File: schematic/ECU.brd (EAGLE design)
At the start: 25 x 79 mm, 21 parts, among them J1 Break, J2 COMM, J3 PWS, J4 DISPLAY, J5 THROTTLE, J6 LED, J7 SPEED, Q1 NMOSFETSOT23, Q5 NMOSFETSOT23

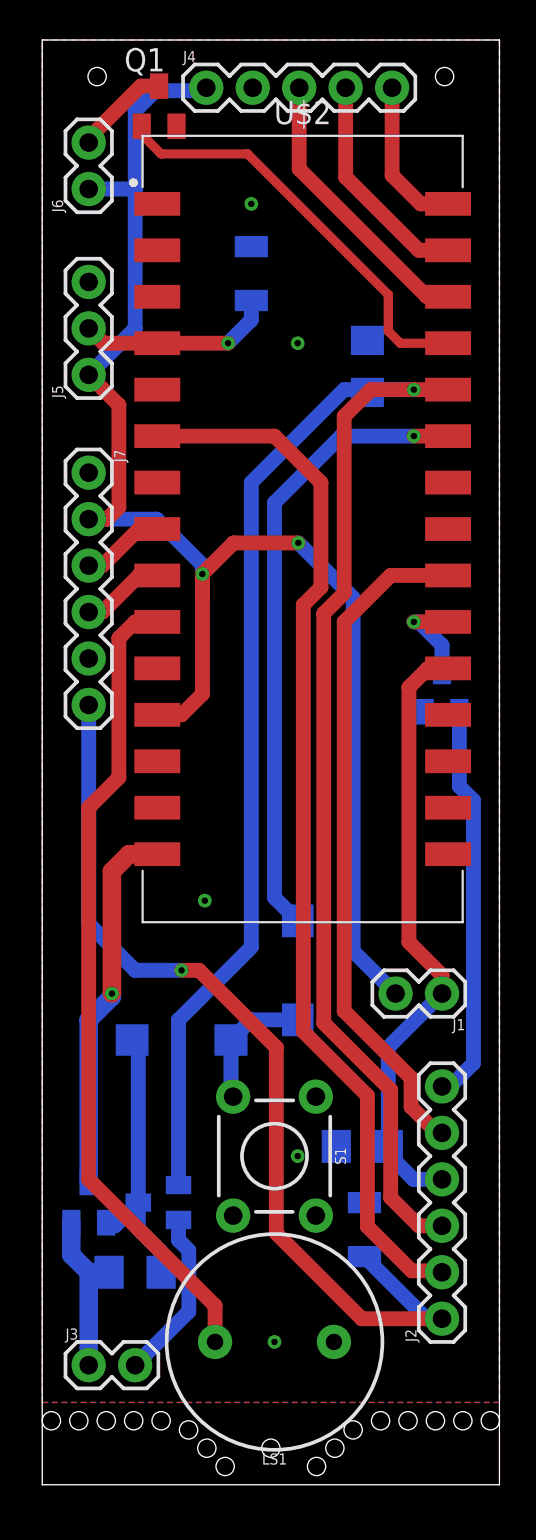
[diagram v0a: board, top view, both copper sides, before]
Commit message: Update schematics
- Add TVS diodes for ESD protection
- Add resistors on MOSFET gates
- Make voltage divider on 2 resistors(4 previously)
- Align signal names on regulator and ECU schematics
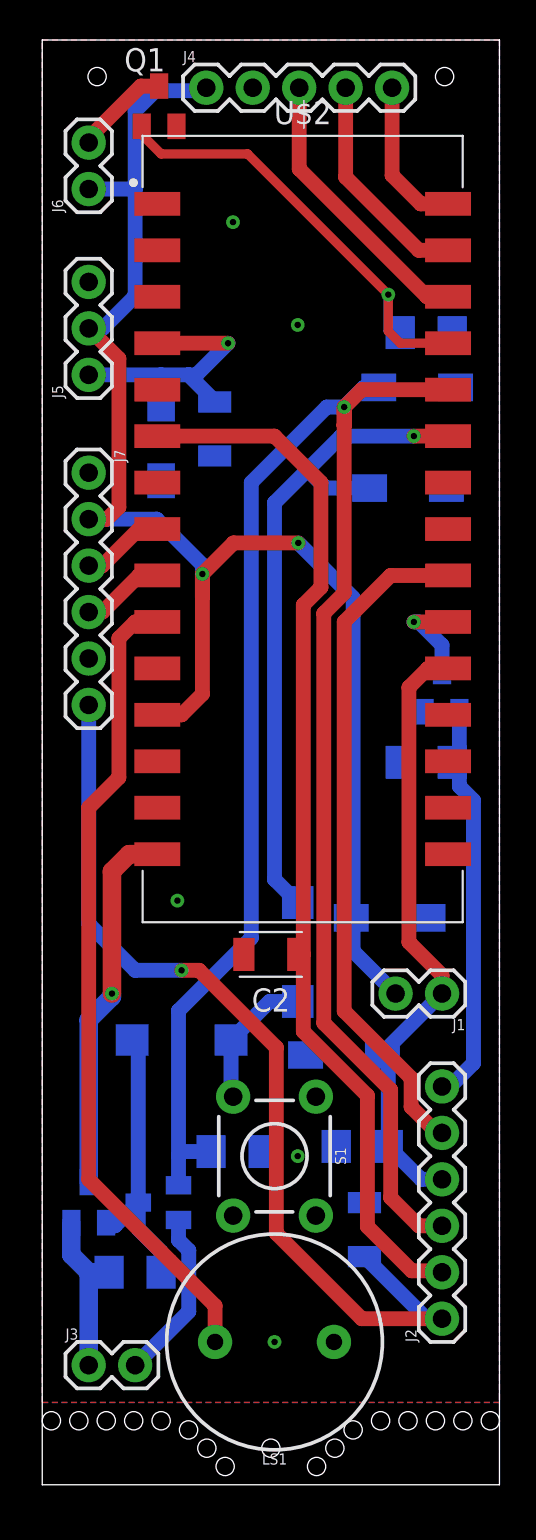
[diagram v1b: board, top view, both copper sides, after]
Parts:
- added C2: (no value), Capacitor:CAPC3216X135
- added D4, D5, D6, D7, U$1: TVS_DIODESMA, eScooter:DIOM5027X220N
- added R4, R5: 10K, eagle-ltspice:R1206
- moved R1 43.5 mm to (10.7, 18.2), turned to 0 degrees
- moved C1 8.73 mm to (9.43, 57.7), turned to 90 degrees
- moved D3 1.00 mm to (14.0, 29.1)
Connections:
- removed net PWR: J2.3, Q2.1, R1.2, U$2.26
- new net PWM: D7.1, J2.3, Q2.1, R1.2, U$2.26
- net 5V: now also D6.1, J5.2; no longer J5.1
- net BAT: now also C2.1
- net BTN: now also U$1.2
- net GND: now also C2.2, D4.1, D5.1, D6.2, D7.2, R4.1, R5.1, U$1.1
- net LEDCTL: now also R5.2
- net SPIN: now also R4.2
- net ST: now also D5.2
- net THIN: now also D4.2, J5.1; no longer J5.2
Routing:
- net PWM: track 0.00 -> 106.8 mm, vias 0 -> 1
- net PWR: track 105.6 -> 0.00 mm, vias 1 -> 0
- net THIN: track 10.8 -> 15.9 mm
- net BTN: track 34.4 -> 37.2 mm
- net LEDCTL: track 23.1 -> 25.8 mm, vias 0 -> 1
- net 5V: track 83.6 -> 84.1 mm

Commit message: Update schematics for regulator
- Add elements nominals and correct values
- Fix library inconsistence
- Few cosmetical changes in schematics
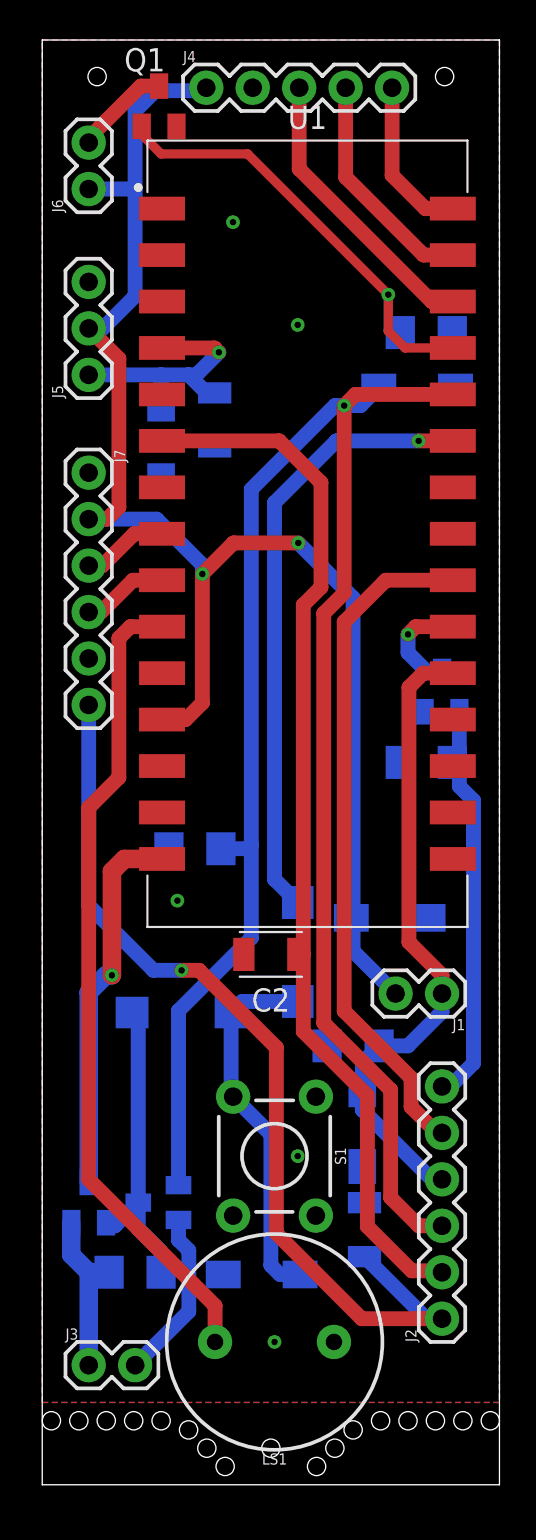
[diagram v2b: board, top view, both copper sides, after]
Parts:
- removed U$1: TVS_DIODESMA, eScooter:DIOM5027X220N
- removed U$2: ARDUINOARDUINO_NANO, regulator:SON254P1750X4300X120-30M
- added D8: TVS_DIODESMA, eScooter:DIOM5027X220N
- added U1: Arduino Nano Every, eScooter:SON254P1750X4300X120-30M
- C1, C2, C3: value (none) -> 0.1uF
- J3: value PWS -> PWR
- R3: value 1M -> 10K
- moved R1 16.7 mm to (8.35, 34.8), turned to 180 degrees
- moved R3 5.52 mm to (17.0, 24.0)
- moved D5 4.12 mm to (17.5, 19.5), turned to 90 degrees
- moved D2 1.50 mm to (7.62, 25.8)
- moved C1 0.50 mm to (9.43, 58.2)
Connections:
- net 3V3: now also U1.2; no longer U$2.2
- net 5V: now also U1.12; no longer U$2.12
- net BAT: now also U1.6; no longer U$2.6
- net BTN: now also U1.25; no longer U$1.2, U$2.25
- net CLK: now also U1.30; no longer U$2.30
- net CS: now also U1.29; no longer U$2.29
- net DIN: now also U1.28; no longer U$2.28
- net GND: now also D8.1, U1.14; no longer U$1.1, U$2.14
- net GND2: now also U1.19; no longer U$2.19
- net LEDCTL: now also U1.27; no longer U$2.27
- net N$5: now also D8.2
- net PWM: now also U1.26; no longer U$2.26
- net SCL: now also U1.9; no longer U$2.9
- net SDA: now also U1.8; no longer U$2.8
- net SP: now also U1.21; no longer U$2.21
- net SPK: now also U1.10; no longer U$2.10
- net ST: now also U1.20; no longer U$2.20
- net STLEDCTL: now also U1.22; no longer U$2.22
- net THIN: now also U1.4; no longer U$2.4
- net VIN: now also U1.15; no longer U$2.15
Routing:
- net N$5: track 7.66 -> 20.4 mm
- net BTN: track 37.2 -> 33.5 mm
- net THIN: track 15.9 -> 14.3 mm
- net N$2: track 15.7 -> 17.2 mm
- net ST: track 33.8 -> 35.2 mm
- net 5V: track 84.1 -> 83.0 mm
- net PWM: track 106.8 -> 105.7 mm
- net SPOUT: track 51.8 -> 51.2 mm

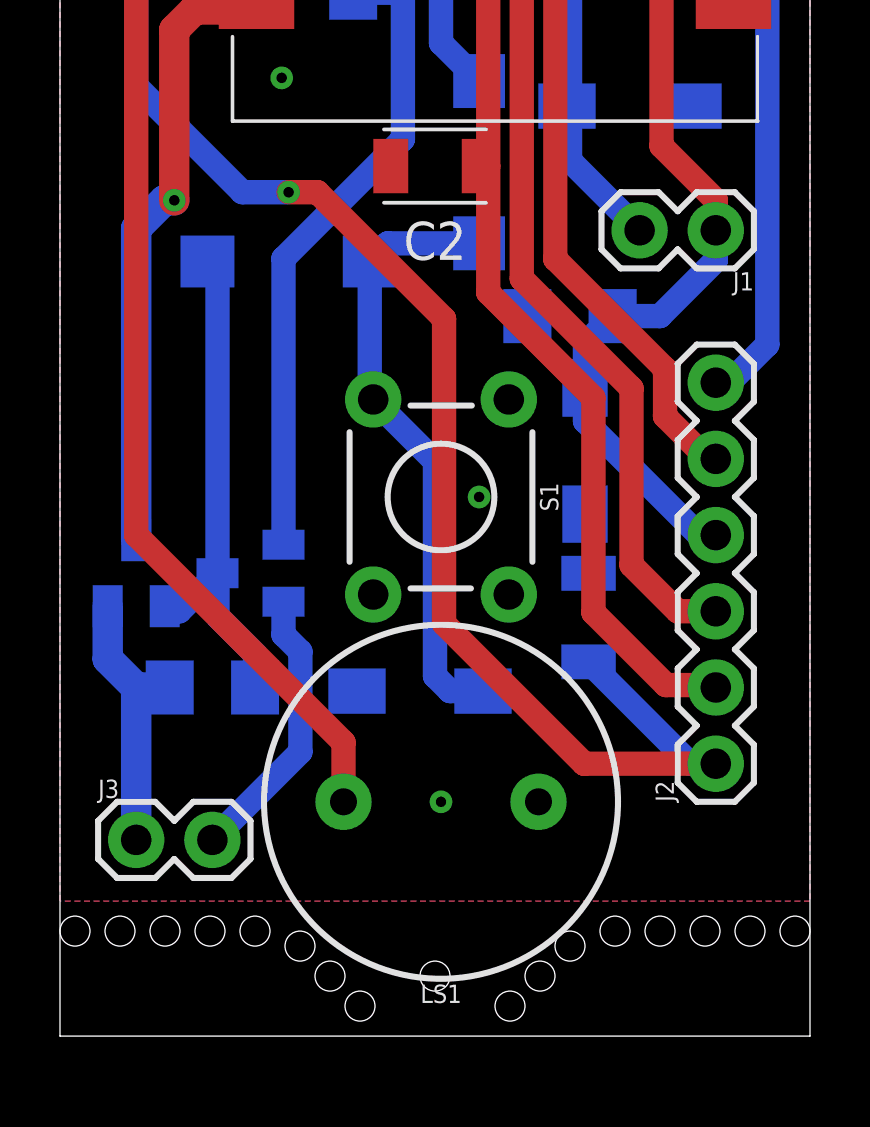
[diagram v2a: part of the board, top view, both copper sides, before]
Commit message: Replace buzzer with 7.6mm contacts spacing
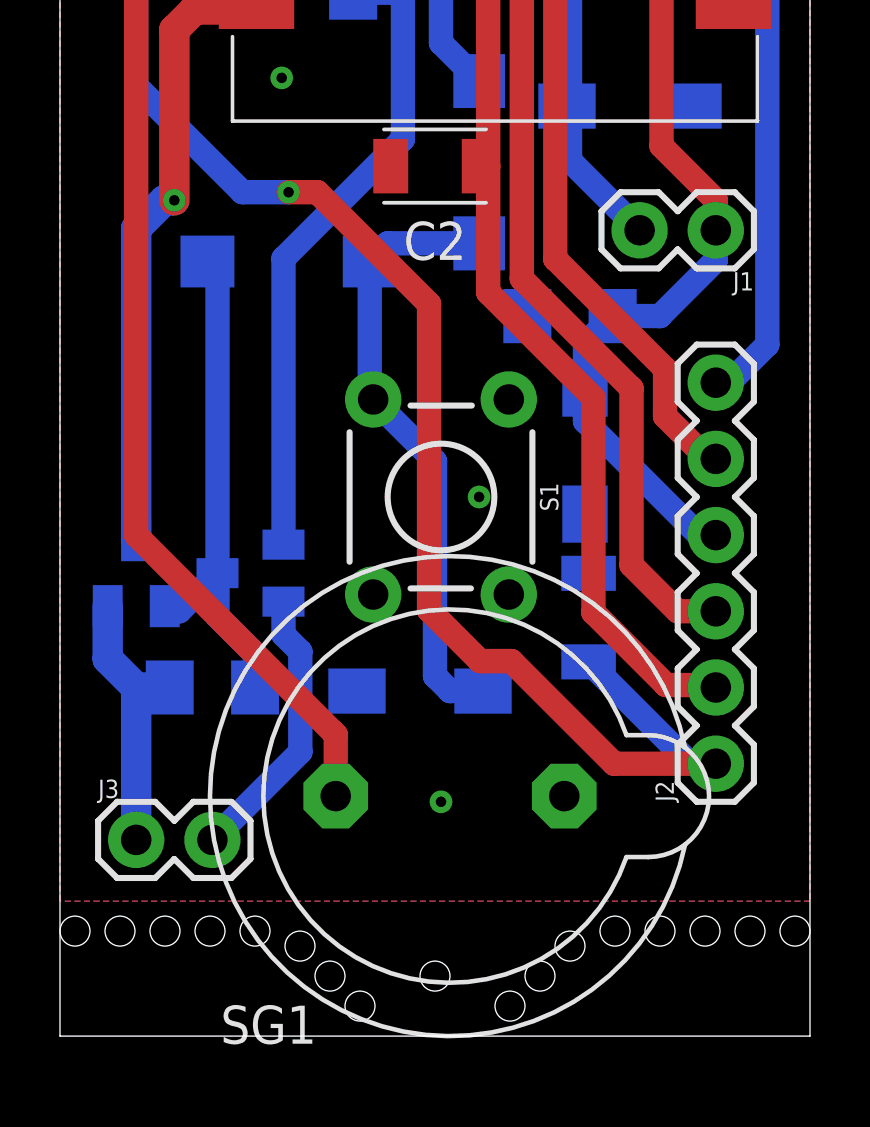
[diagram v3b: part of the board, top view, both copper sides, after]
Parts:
- removed LS1: BUZZER-PTH_KIT, SparkFun-Electromechanical:BUZZER-12MM-KIT
- added SG1: F/HGP, buzzer:F/HGP
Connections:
- net GND: now also SG1.1; no longer LS1.-
- net SPK: now also SG1.2; no longer LS1.+
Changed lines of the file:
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@@
 <attribute name="VALUE" x="9.525" y="17.97" size="0.6096" layer="27" font="vector" ratio="20" rot="R270" align="top-center"/>
-</element>
-<element name="LS1" library="SparkFun-Electromechanical" library_urn="urn:adsk.eagle:library:516" package="BUZZER-12MM-KIT" package3d_urn="urn:adsk.eagle:package:38556/1" value="BUZZER-PTH_KIT" x="12.7" y="7.81" smashed="yes" rot="R180">
-<attribute name="NAME" x="12.7" y="1.714" size="0.6096" layer="25" font="vector" ratio="20" rot="R180" align="bottom-center"/>
-<attribute name="PROD_ID" value="COMP-08253" x="12.7" y="7.81" size="1.778" layer="27" rot="R180" display="off"/>
-<attribute name="SF_SKU" value="COM-07950" x="12.7" y="7.81" size="1.778" layer="27" rot="R180" display="off"/>
-<attribute name="VALUE" x="12.7" y="2.222" size="0.6096" layer="27" font="vector" ratio="20" rot="R180" align="top-center"/>
 </element>
 <element name="R3" library="eagle-ltspice" library_urn="urn:adsk.eagle:library:217" package="R1206" package3d_urn="urn:adsk.eagle:package:13301/1" value="10K" x="17" y="24" smashed="yes" rot="MR0">
@@
 <attribute name="NAME" x="14.5" y="74.135" size="1.27" layer="25" align="bottom-center"/>
 <attribute name="VALUE" x="14.5" y="29.865" size="1.27" layer="27" align="top-center"/>
+</element>
+<element name="SG1" library="buzzer" library_urn="urn:adsk.eagle:library:113" package="F/HGP" package3d_urn="urn:adsk.eagle:package:5287/1" value="F/HGP" x="13" y="8" smashed="yes" rot="R180">
+<attribute name="MF" value="" x="13" y="8" size="1.778" layer="27" rot="R180" display="off"/>
+<attribute name="MPN" value="" x="13" y="8" size="1.778" layer="27" rot="R180" display="off"/>
+<attribute name="NAME" x="8.555" y="1.015" size="1.27" layer="25" ratio="10" rot="R180"/>
+<attribute name="OC_FARNELL" value="unknown" x="13" y="8" size="1.778" layer="27" rot="R180" display="off"/>
+<attribute name="OC_NEWARK" value="unknown" x="13" y="8" size="1.778" layer="27" rot="R180" display="off"/>
+<attribute name="POPULARITY" value="0" x="13" y="8" size="1.778" layer="27" rot="R180" display="off"/>
+<attribute name="VALUE" x="16.683" y="11.81" size="1.27" layer="27" ratio="10" rot="R180"/>
 </element>
 </elements>
@@
 <via x="13.97" y="17.97" extent="1-16" drill="0.35"/>
 <via x="12.7" y="7.81" extent="1-16" drill="0.35"/>
-<contactref element="LS1" pad="-"/>
 <wire x1="7.45" y1="14.48" x2="7.45" y2="13.3792875" width="0.8128" layer="16"/>
 <wire x1="7.45" y1="13.3792875" x2="8.0132" y2="12.8160875" width="0.8128" layer="16"/>
@@
 <contactref element="C2" pad="2"/>
 <contactref element="U1" pad="14"/>
+<contactref element="SG1" pad="1"/>
 </signal>
 <signal name="VIN">
@@
 <contactref element="J7" pad="6"/>
 <contactref element="C3" pad="1"/>
-<wire x1="12.8016" y1="23.90786875" x2="12.8016" y2="13.74786875" width="0.8128" layer="1"/>
+<wire x1="12.3016" y1="24.40786875" x2="12.3016" y2="14.1984" width="0.8128" layer="1"/>
 <wire x1="2.54" y1="31.67" x2="6.08" y2="28.13" width="0.8128" layer="16"/>
 <wire x1="7.62" y1="28.13" x2="8.57946875" y2="28.13" width="0.8128" layer="1"/>
-<wire x1="8.57946875" y1="28.13" x2="12.8016" y2="23.90786875" width="0.8128" layer="1"/>
+<wire x1="8.57946875" y1="28.13" x2="12.3016" y2="24.40786875" width="0.8128" layer="1"/>
 <wire x1="2.54" y1="42.64" x2="2.54" y2="31.67" width="0.8128" layer="16"/>
 <via x="7.62" y="28.13" extent="1-16" drill="0.35"/>
 <wire x1="6.08" y1="28.13" x2="7.62" y2="28.13" width="0.8128" layer="16"/>
 <contactref element="J2" pad="1"/>
-<wire x1="12.8016" y1="13.74786875" x2="17.46946875" y2="9.08" width="0.8128" layer="1"/>
-<wire x1="17.46946875" y1="9.08" x2="21.86" y2="9.08" width="0.8128" layer="1"/>
+<wire x1="12.3016" y1="14.1984" x2="14" y2="12.5" width="0.8128" layer="1"/>
+<wire x1="18.46946875" y1="9.08" x2="21.86" y2="9.08" width="0.8128" layer="1"/>
 <wire x1="21.0146" y1="9.08" x2="21.86" y2="9.08" width="0.8128" layer="16"/>
 <wire x1="17.62" y1="12.4746" x2="21.0146" y2="9.08" width="0.8128" layer="16"/>
+<wire x1="15.04946875" y1="12.5" x2="18.46946875" y2="9.08" width="0.8128" layer="1"/>
+<wire x1="14" y1="12.5" x2="15.04946875" y2="12.5" width="0.8128" layer="1"/>
 </signal>
 <signal name="SPK">
-<contactref element="LS1" pad="+"/>
 <wire x1="2.54" y1="37.02" x2="2.54" y2="16.7" width="0.8128" layer="1"/>
-<wire x1="9.45" y1="9.79" x2="9.45" y2="7.81" width="0.8128" layer="1"/>
-<wire x1="2.54" y1="16.7" x2="9.45" y2="9.79" width="0.8128" layer="1"/>
+<wire x1="2.54" y1="16.7" x2="9.12" y2="10.12" width="0.8128" layer="1"/>
 <wire x1="2.54" y1="37.02" x2="4.191" y2="38.671" width="0.8128" layer="1"/>
 <wire x1="4.191" y1="46.291" x2="4.191" y2="38.671" width="0.8128" layer="1"/>
@@
 <wire x1="6.55" y1="46.92" x2="4.82" y2="46.92" width="0.8128" layer="1"/>
 <wire x1="4.82" y1="46.92" x2="4.191" y2="46.291" width="0.8128" layer="1"/>
+<contactref element="SG1" pad="2"/>
+<wire x1="9.19" y1="8" x2="9.19" y2="10.05" width="0.8128" layer="1"/>
+<wire x1="9.19" y1="10.05" x2="9.12" y2="10.12" width="0.8128" layer="1"/>
 </signal>
 <signal name="3V3">
